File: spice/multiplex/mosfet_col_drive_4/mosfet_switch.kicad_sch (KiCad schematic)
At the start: 13 parts, among them Q1 NPN, Q2 PMOS

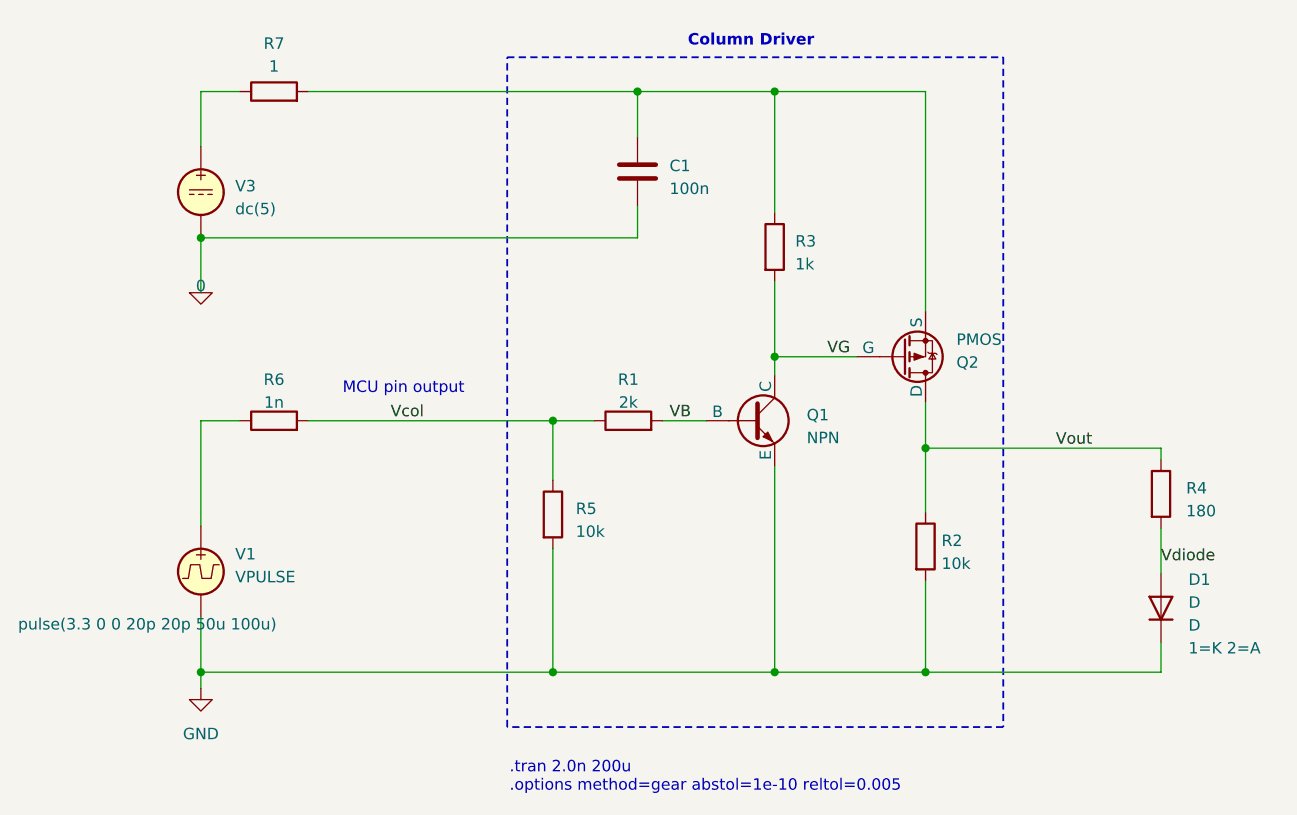
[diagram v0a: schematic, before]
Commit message: Worked on spice models.
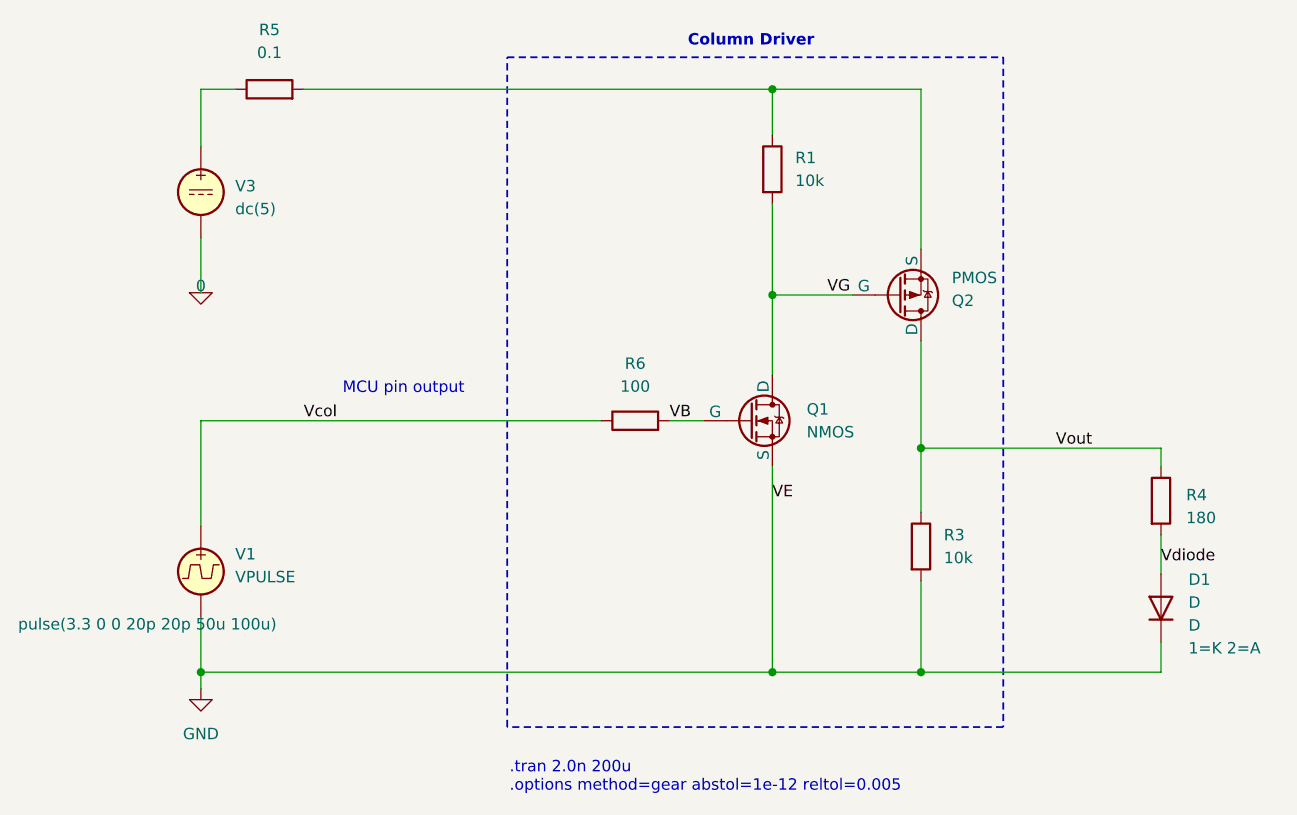
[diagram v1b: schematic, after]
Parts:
- removed C1: 100n, symbol Device:C
- removed Q1: NPN, symbol Simulation_SPICE:NPN
- removed R1: 2k, symbol Device:R
- removed R5: 10k, symbol Device:R
- added Q1: NMOS, symbol Simulation_SPICE:NMOS
- R1: renamed from R3; value 1k -> 10k
- R5: renamed from R7; value 1 -> 0.1
- R6: value 1n -> 100
- renumbered R2 to R3
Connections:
- net GND: now also Q1.3 (S)
- net VB: now also R6.2, Q1.2 (G)
- net VG: now also Q1.1 (D)
- net Vcol: now also R6.1, V1.1; no longer R6.2
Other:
- note added: ".tran 2.0n 200u .options method=gear abstol=1e-12 reltol=0.005"
- note removed: ".tran 2.0n 200u .options method=gear abstol=1e-10 reltol=0.005"
- moved on the sheet: Q2, R1, R3, R4, R5, R6
